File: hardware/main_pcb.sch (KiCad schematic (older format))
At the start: 67 parts

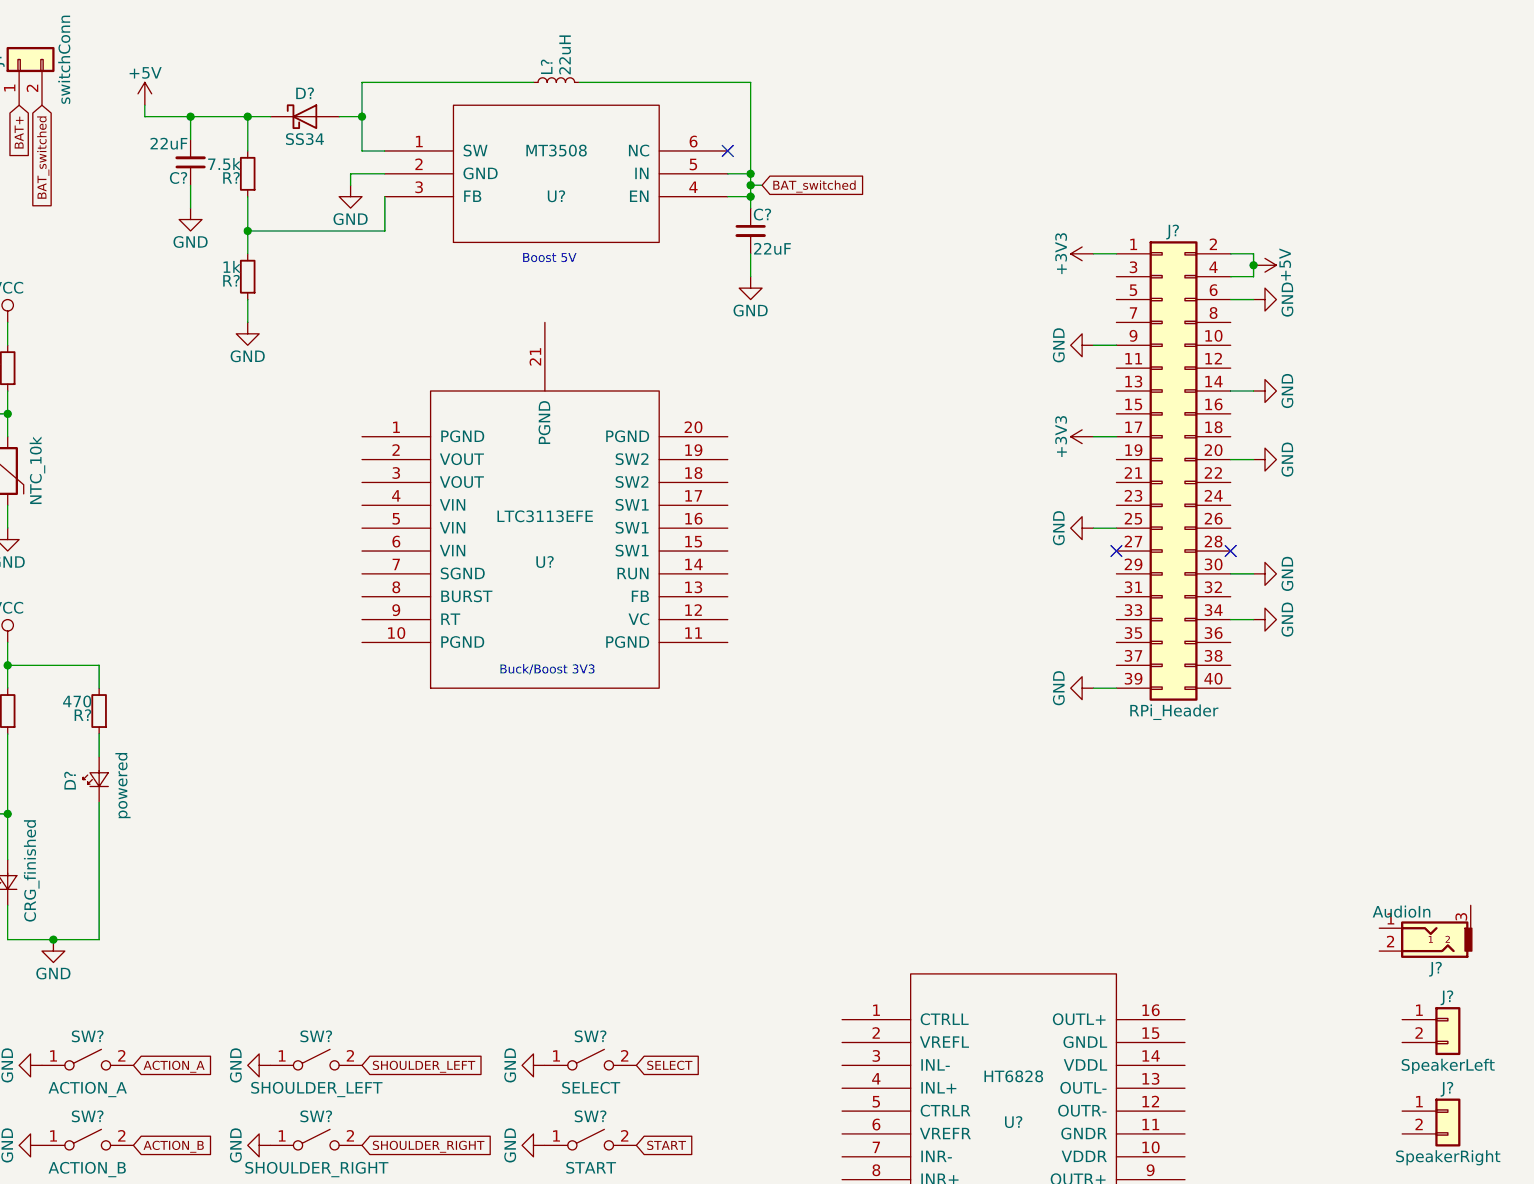
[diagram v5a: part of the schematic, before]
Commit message: schematic update
added B103 dual audio poti
added Buck/Boost Circuit
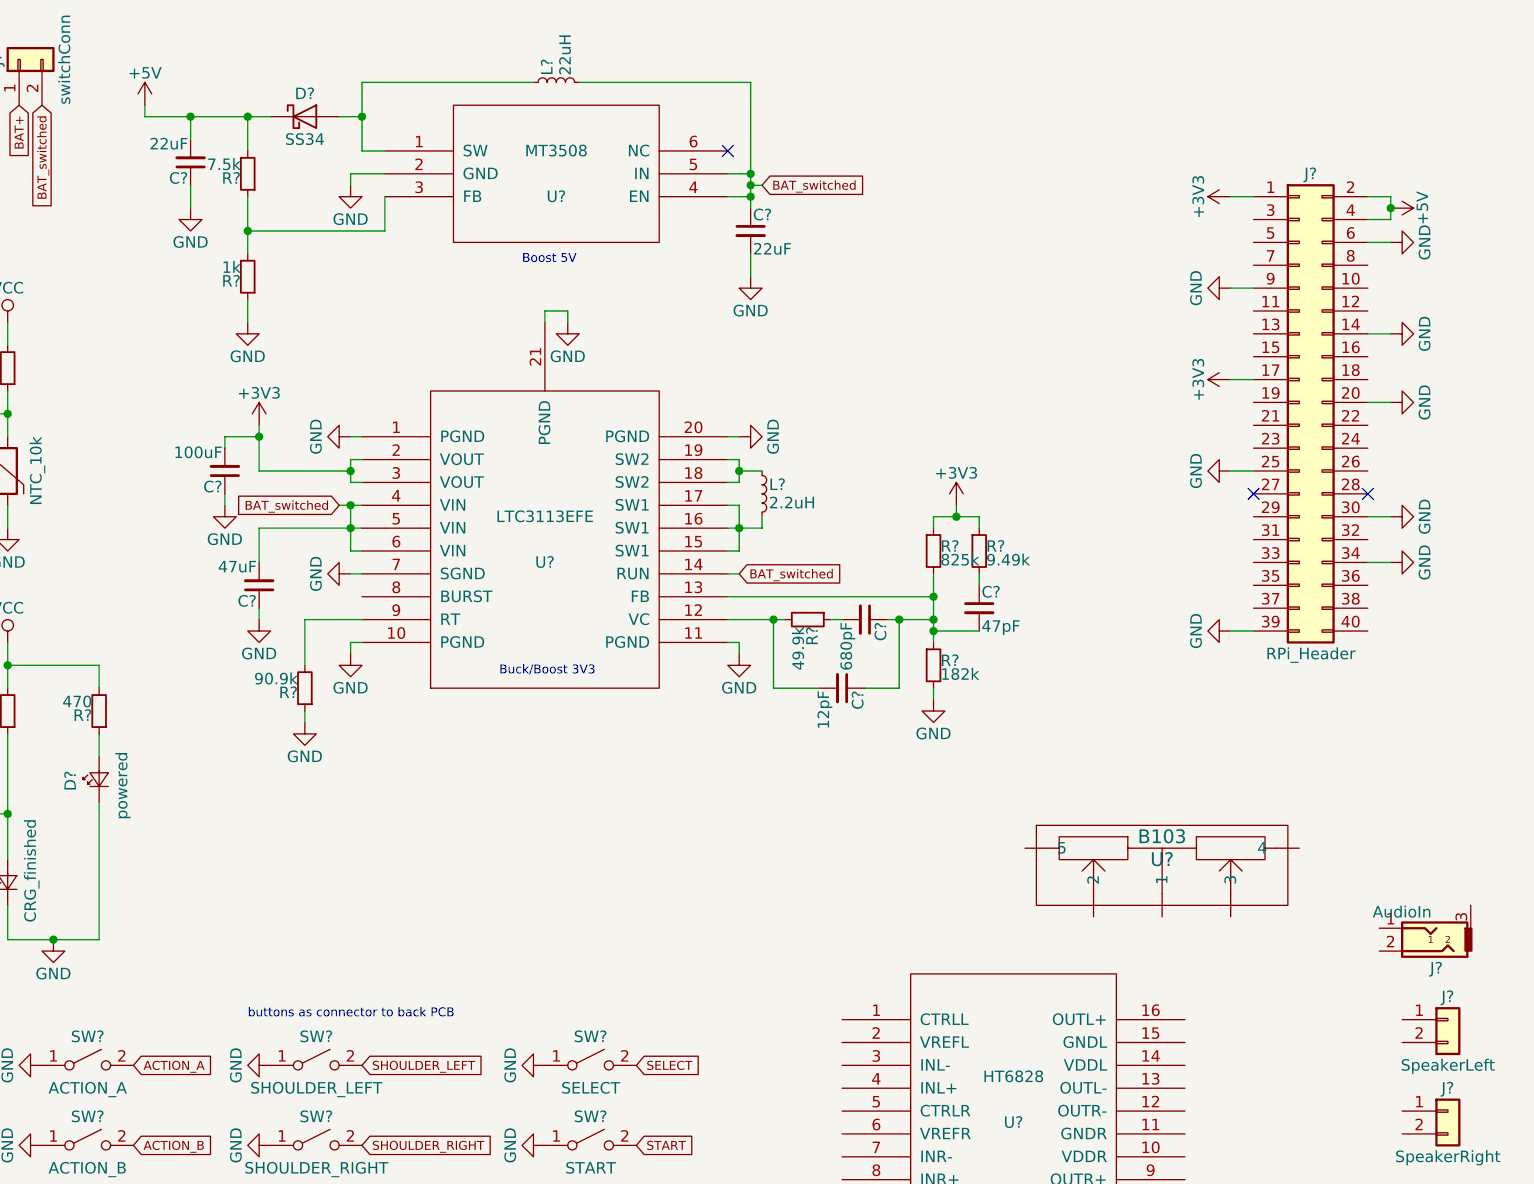
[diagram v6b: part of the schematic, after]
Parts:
- added C?: 680pF, symbol C_Small
- added C?: 12pF, symbol C_Small
- added C?: 47pF, symbol C_Small
- added C?: 100uF, symbol C_Small
- added C?: 47uF, symbol C_Small
- added L?: 2.2uH, symbol L_Small
- added R?: 49.9k, symbol R_Small
- added R?: 182k, symbol R_Small
- added R?: 825k, symbol R_Small
- added R?: 9.49k, symbol R_Small
- added R?: 90.9k, symbol R_Small
- added U?: B103, symbol B103
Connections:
- net +3V3: now also U?.2 (VOUT), U?.3 (VOUT), C?.2, R?.1, R?.1
- net BAT_switched: now also U?.14 (RUN), U?.4 (VIN), U?.5 (VIN), U?.6 (VIN), C?.2
- net GND: now also U?.1 (PGND), U?.10 (PGND), U?.11 (PGND), U?.20 (PGND), U?.21 (PGND), U?.7 (SGND), C?.1, C?.1, R?.1, R?.2
- net at U?.12 (VC): now also C?.2, R?.2
- net at U?.13 (FB): now also C?.1, C?.1, C?.2, R?.1, R?.2
- net at U?.15 (SW1): now also U?.16 (SW1), U?.17 (SW1), L?.2
- net at U?.18 (SW2): now also U?.19 (SW2), L?.1
- net at U?.9 (RT): now also R?.2
- new net: C?.2, R?.1
- new net: C?.1, R?.2
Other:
- note added: "buttons as connector to back PCB"
- moved on the sheet: J?

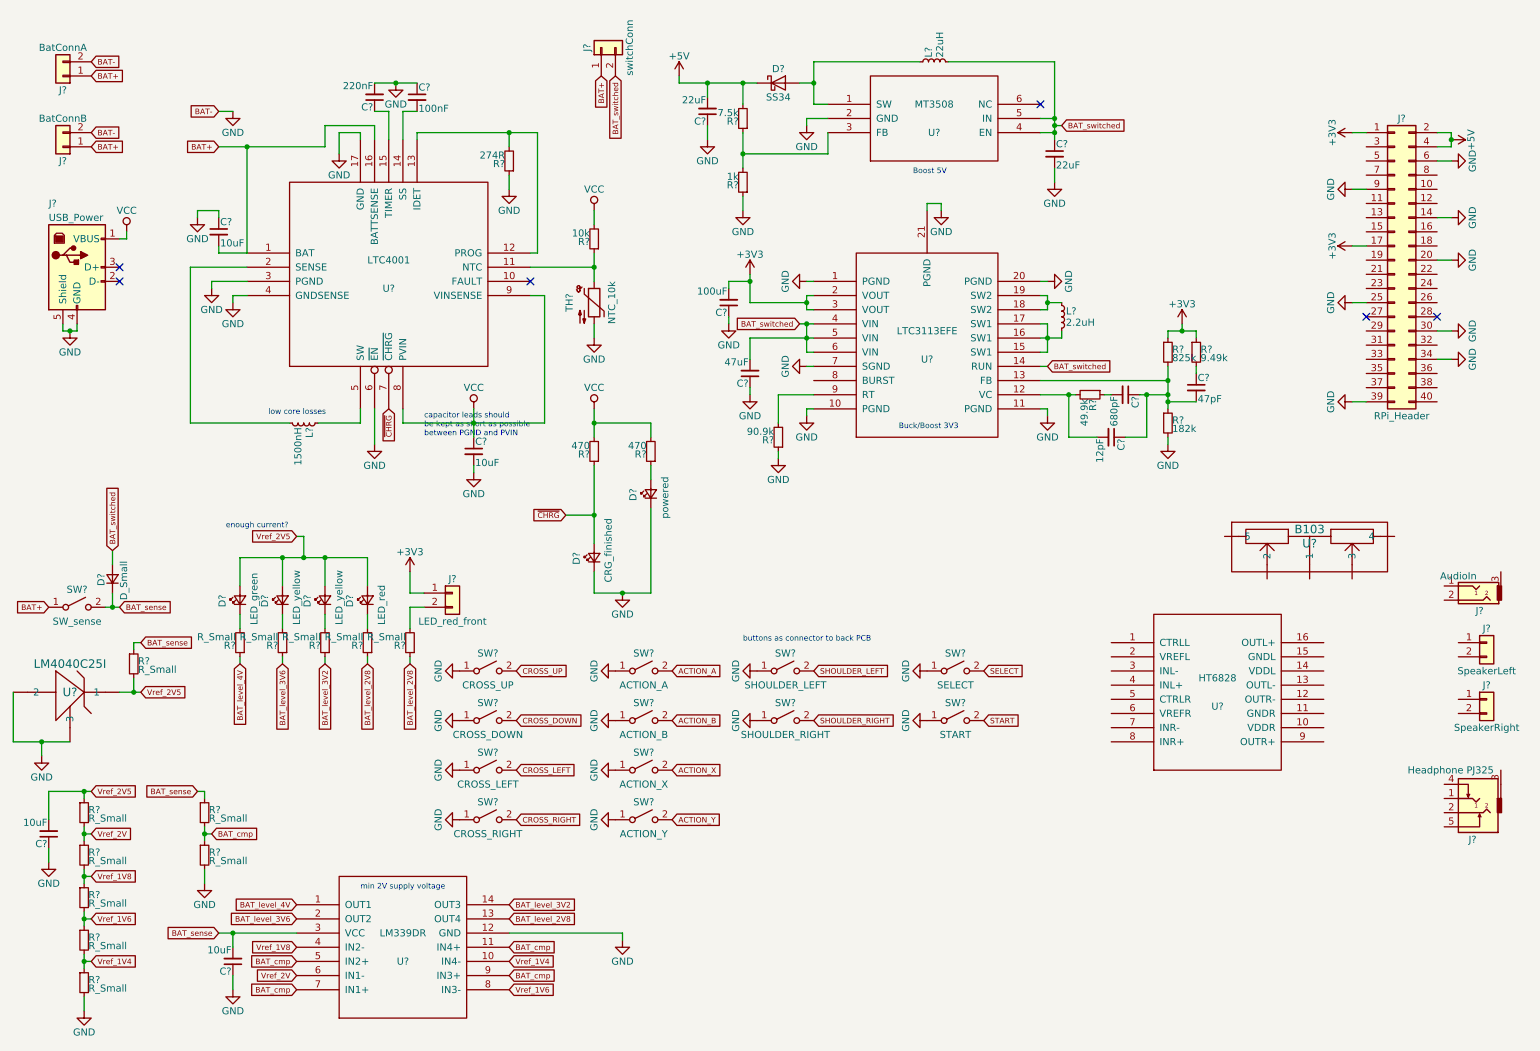
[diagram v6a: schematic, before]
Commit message: datasheets and schematic updates
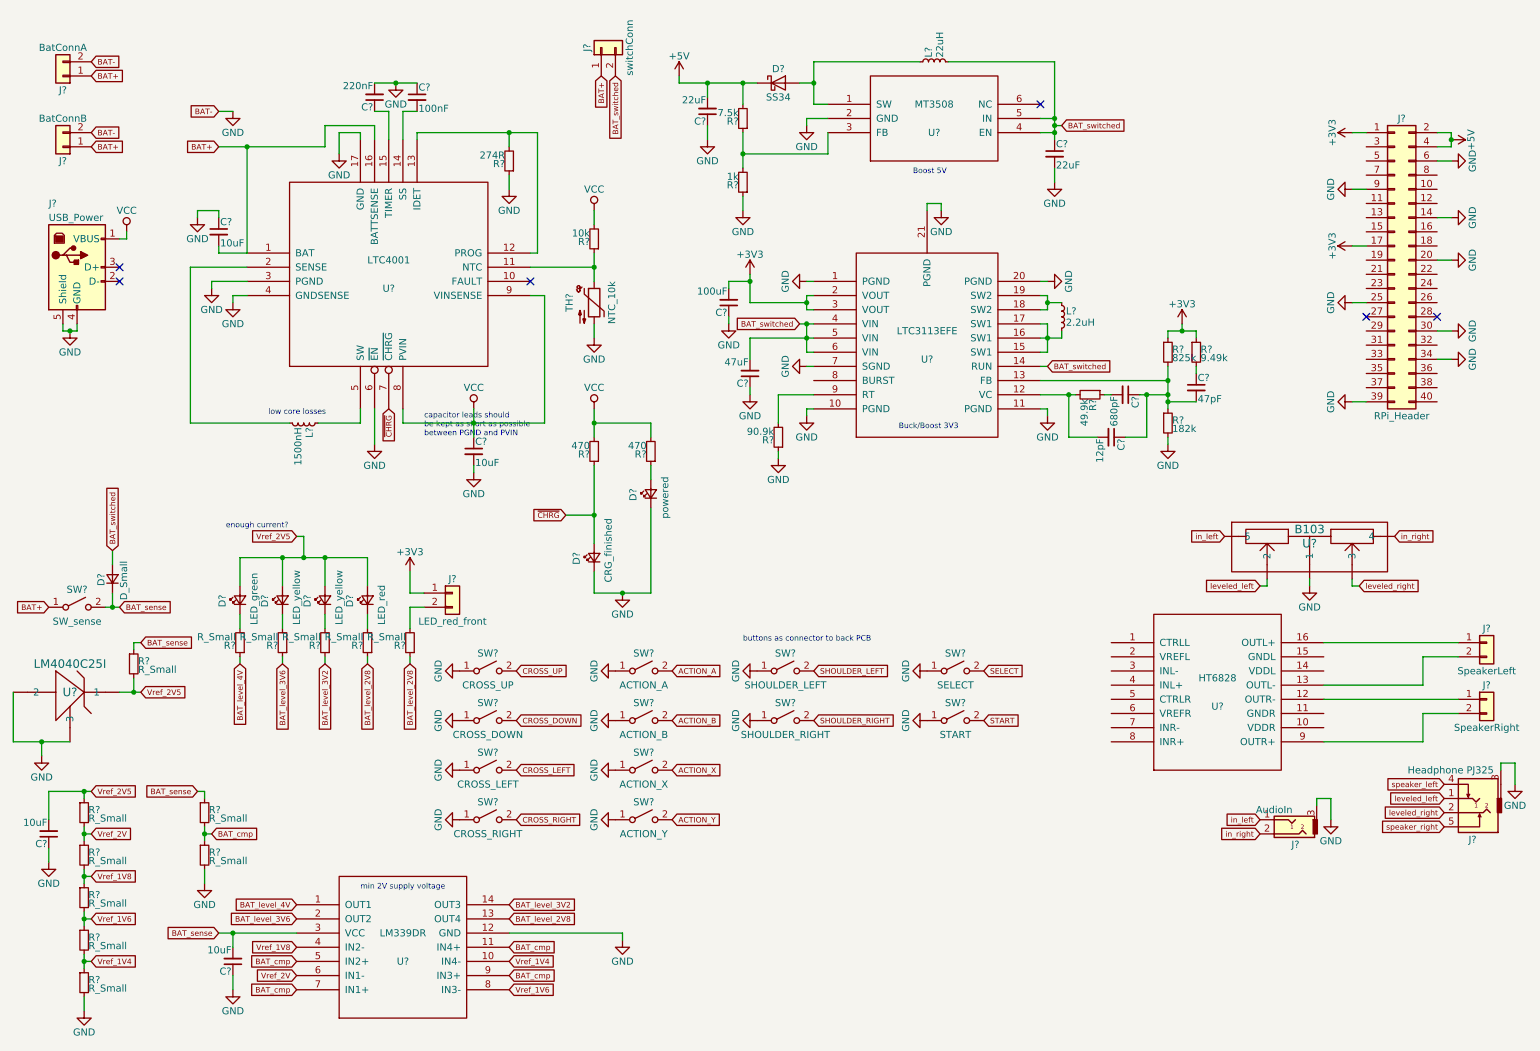
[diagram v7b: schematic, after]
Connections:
- net GND: now also J?.3, J?.3, U?.~ (5)
- net at U?.12 (OUTR-): now also J?.1 (Pin_1)
- net at U?.13 (OUTL-): now also J?.2 (Pin_2)
- net at U?.16 (OUTL+): now also J?.1 (Pin_1)
- net at U?.9 (OUTR+): now also J?.2 (Pin_2)
- net leveled_left: now reaches J?.1
- net leveled_left: now also U?.~ (5)
- net leveled_right: now reaches J?.2
- net leveled_right: now also U?.~ (5)
- net speaker_left: now reaches J?.4
- net speaker_right: now reaches J?.5
- net in_left: now reaches J?.1
- net in_left: now also U?.~ (5)
- net in_right: now reaches J?.2
- net in_right: now also U?.~ (5)
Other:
- moved on the sheet: J?
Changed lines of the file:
@@
 L Audio-Jack-3 J?
 U 1 1 5A6347BA
-P 10850 4550
-F 0 "J?" H 10800 4725 50  0000 C CNN
-F 1 "AudioIn" H 10950 4480 50  0000 C CNN
-F 2 "" H 11100 4650 50  0001 C CNN
-F 3 "" H 11100 4650 50  0001 C CNN
-	1    10850 4550
+P 9550 6200
+F 0 "J?" H 9500 6375 50  0000 C CNN
+F 1 "AudioIn" H 9650 6130 50  0000 C CNN
+F 2 "" H 9800 6300 50  0001 C CNN
+F 3 "" H 9800 6300 50  0001 C CNN
+	1    9550 6200
 	-1   0    0    1
 $EndComp
@@
 	2200 2200 2200 1450
 Wire Wire Line
-	2750 1450 2000 1450
-Wire Wire Line
-	2750 1300 2750 1450
+	2000 1450 2750 1450
+Wire Wire Line
+	2750 1450 2750 1300
 Connection ~ 2200 1450
 Wire Wire Line
@@
 	3100 1300 3100 1400
 Wire Wire Line
-	3100 1300 2750 1300
+	2750 1300 3100 1300
 Wire Wire Line
 	3000 1400 3000 1350
@@
 	1050 7550 1050 7450
 Wire Wire Line
-	1050 7250 1050 7150
-Wire Wire Line
-	1050 6950 1050 6850
-Wire Wire Line
-	1050 6650 1050 6550
-Wire Wire Line
-	1050 6350 1050 6250
+	1050 7150 1050 7250
+Wire Wire Line
+	1050 6850 1050 6950
+Wire Wire Line
+	1050 6550 1050 6650
+Wire Wire Line
+	1050 6250 1050 6350
 Wire Wire Line
 	1050 6050 1050 6000
@@
 	1900 6650 1900 6550
 Wire Wire Line
-	1900 6350 1900 6250
+	1900 6250 1900 6350
 Wire Wire Line
 	1900 6050 1900 6000
@@
 Connection ~ 5700 1500
 Wire Wire Line
-	5700 1150 5700 1000
+	5700 1000 5700 1150
 Wire Wire Line
 	5250 1000 5800 1000
@@
 	6150 2400 6200 2400
 Wire Wire Line
-	6200 2900 6150 2900
-Wire Wire Line
-	6150 2900 6150 2700
+	6150 2900 6200 2900
+Wire Wire Line
+	6150 2700 6150 2900
 Wire Wire Line
 	6100 2700 6200 2700
@@
 BAT_switched
 Wire Wire Line
-	6200 2600 6150 2600
-Wire Wire Line
-	6150 2600 6150 2500
+	6150 2600 6200 2600
+Wire Wire Line
+	6150 2500 6150 2600
 Wire Wire Line
 	6150 2500 6200 2500
@@
 $EndComp
 Wire Wire Line
-	8050 3200 7800 3200
+	7800 3200 8050 3200
 Wire Wire Line
 	8250 3200 8300 3200
@@
 	8700 3000 8700 3300
 Wire Wire Line
-	8700 3200 8500 3200
+	8500 3200 8700 3200
 Wire Wire Line
 	8400 3500 8550 3500
@@
 Connection ~ 8700 3250
 Wire Wire Line
-	8900 2800 8900 2750
-Wire Wire Line
-	8900 2750 8700 2750
+	8900 2750 8900 2800
+Wire Wire Line
+	8700 2750 8900 2750
 Wire Wire Line
 	8700 2750 8700 2800
@@
 	1    0    0    -1
 $EndComp
+$Comp
+L GND #PWR?
+U 1 1 5A67B65A
+P 11150 5950
+F 0 "#PWR?" H 11150 5700 50  0001 C CNN
+F 1 "GND" H 11150 5800 50  0000 C CNN
+F 2 "" H 11150 5950 50  0001 C CNN
+F 3 "" H 11150 5950 50  0001 C CNN
+	1    11150 5950
+	1    0    0    -1
+$EndComp
+$Comp
+L GND #PWR?
+U 1 1 5A67C13B
+P 9850 6200
+F 0 "#PWR?" H 9850 5950 50  0001 C CNN
+F 1 "GND" H 9850 6050 50  0000 C CNN
+F 2 "" H 9850 6200 50  0001 C CNN
+F 3 "" H 9850 6200 50  0001 C CNN
+	1    9850 6200
+	1    0    0    -1
+$EndComp
+$Comp
+L GND #PWR?
+U 1 1 5A67D1AA
+P 9700 4550
+F 0 "#PWR?" H 9700 4300 50  0001 C CNN
+F 1 "GND" H 9700 4400 50  0000 C CNN
+F 2 "" H 9700 4550 50  0001 C CNN
+F 3 "" H 9700 4550 50  0001 C CNN
+	1    9700 4550
+	1    0    0    -1
+$EndComp
+Wire Wire Line
+	9700 4550 9700 4500
+Wire Wire Line
+	9750 6100 9750 6050
+Wire Wire Line
+	9750 6050 9850 6050
+Wire Wire Line
+	9850 6050 9850 6200
+Wire Wire Line
+	11050 5850 11050 5800
+Wire Wire Line
+	11050 5800 11150 5800
+Wire Wire Line
+	11150 5800 11150 5950
+Wire Wire Line
+	9800 5250 10500 5250
+Wire Wire Line
+	10500 5250 10500 5050
+Wire Wire Line
+	10500 5050 10750 5050
+Wire Wire Line
+	9800 4950 10750 4950
+Wire Wire Line
+	9800 5350 10750 5350
+Wire Wire Line
+	10750 5450 10500 5450
+Wire Wire Line
+	10500 5450 10500 5650
+Wire Wire Line
+	10500 5650 9800 5650
+Text GLabel 9350 6200 0    39   Input ~ 0
+in_left
+Text GLabel 9350 6300 0    39   Input ~ 0
+in_right
+Text GLabel 9100 4200 0    39   Input ~ 0
+in_left
+Text GLabel 10300 4200 2    39   Input ~ 0
+in_right
+Text GLabel 10050 4550 2    39   Input ~ 0
+leveled_right
+Text GLabel 9350 4550 0    39   Input ~ 0
+leveled_left
+Wire Wire Line
+	9350 4550 9400 4550
+Wire Wire Line
+	9400 4550 9400 4500
+Wire Wire Line
+	10000 4500 10000 4550
+Wire Wire Line
+	10000 4550 10050 4550
+Text GLabel 10650 6150 0    39   Input ~ 0
+leveled_right
+Text GLabel 10650 6050 0    39   Input ~ 0
+leveled_left
+Text GLabel 10650 5950 0    39   Input ~ 0
+speaker_left
+Text GLabel 10650 6250 0    39   Input ~ 0
+speaker_right
 $EndSCHEMATC

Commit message: DUMMIES
added dummies
added datasheets
small updates
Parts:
- added IC?: LM3914N, DIL18, symbol LM3914N
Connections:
- net BAT_sense: no longer D?.1 (K), SW?.2 (B)
- net GND: no longer U?.~ (3)
- new net: D?.1 (K), SW?.2 (B)
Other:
- note removed: "enough current?"
- moved on the sheet: C?, D?, J?, R?, SW?, U?
